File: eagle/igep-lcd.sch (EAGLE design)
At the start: 36 parts, among them IC1 LM1117IMPX-3.3, U1 SN74LVC8T245PW, U2 SN74LVC8T245PW, U3 SN74LVC8T245PW, U4 SN74LVC8T245PW

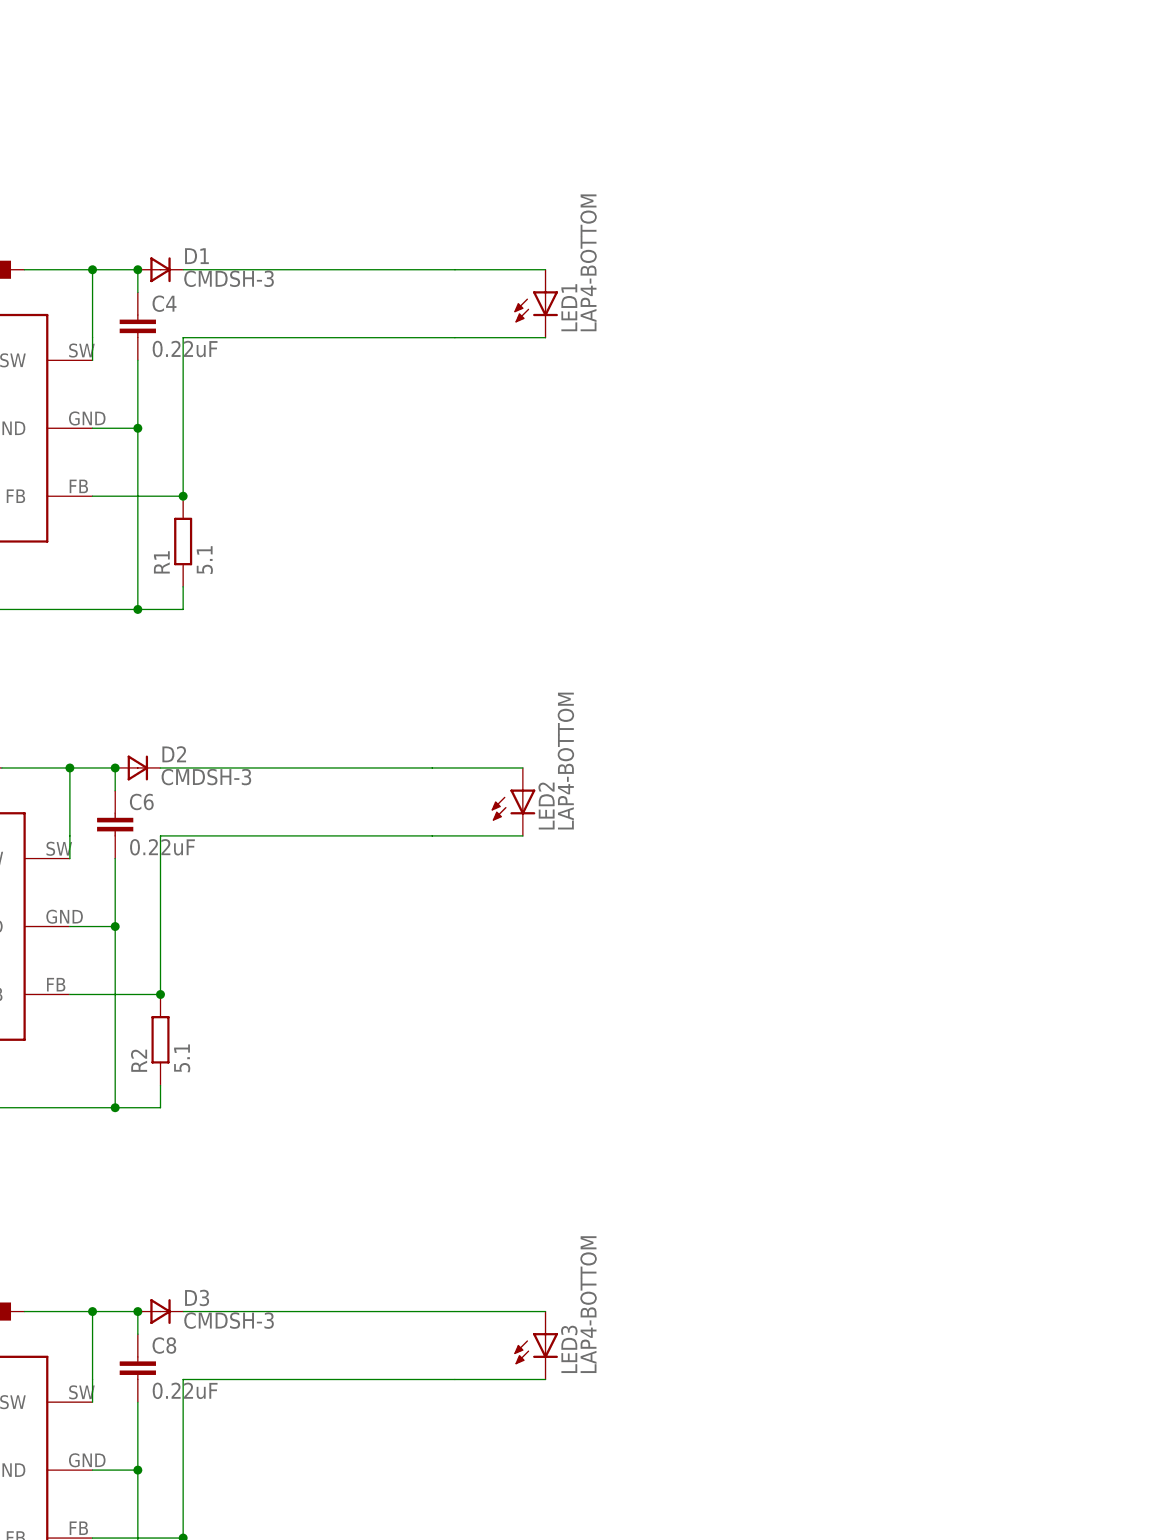
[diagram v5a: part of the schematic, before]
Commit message: Added backlight connectors
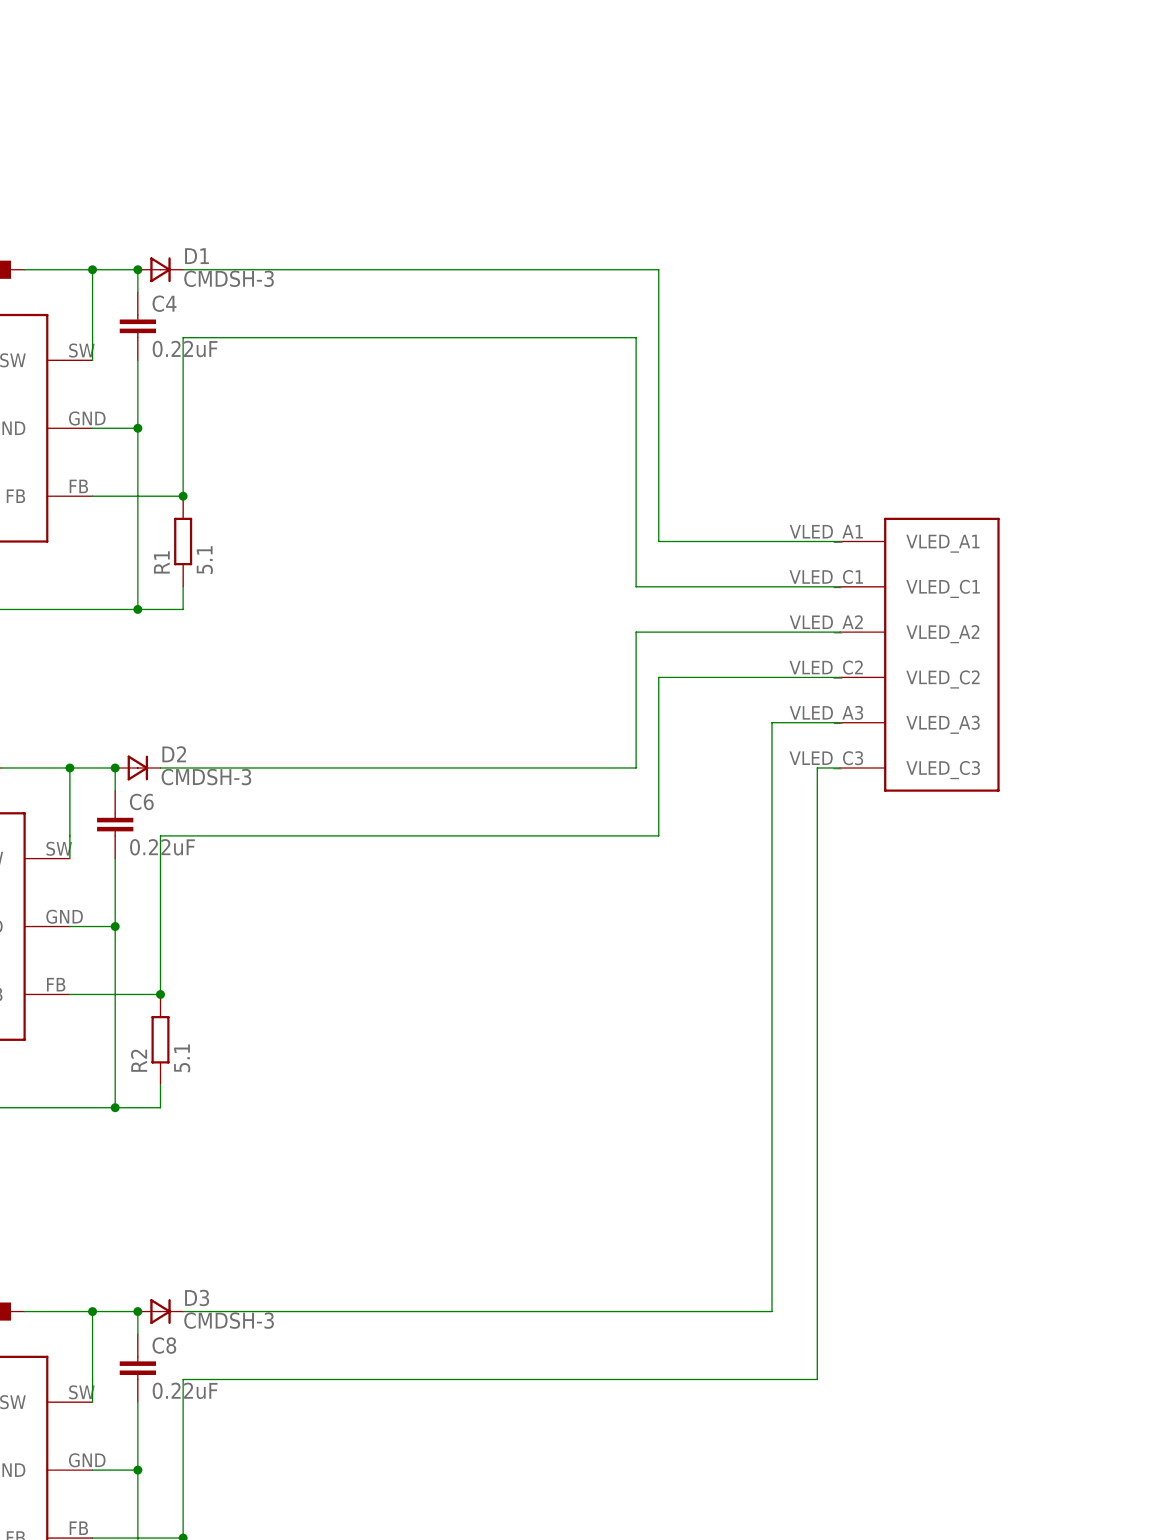
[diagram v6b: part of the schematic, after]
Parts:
- removed LED1, LED2, LED3: LAP4-BOTTOM, led:LAP4-BOTTOM
- added U$5: LCD_BL, lcd-bl:LCD_BL
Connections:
- net N$13: now also U$5.VLED_A1; no longer LED1.A
- net N$14: now also U$5.VLED_C1; no longer LED1.C
- net N$16: now also U$5.VLED_A2; no longer LED2.A
- net N$17: now also U$5.VLED_C2; no longer LED2.C
- net N$22: now also U$5.VLED_A3; no longer LED3.A
- net N$23: now also U$5.VLED_C3; no longer LED3.C
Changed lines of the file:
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@@
 <part name="C4" library="resistor" deviceset="C-EU" device="025-024X044" value="0.22uF"/>
 <part name="R1" library="resistor" deviceset="R-EU_" device="0204/2V" value="5.1"/>
-<part name="LED1" library="led" deviceset="*P4" device="-BOTTOM" technology="LA"/>
 <part name="BL_5VOLT_1" library="testpad" deviceset="TP" device="B1,27"/>
 <part name="BL_PWM_1" library="testpad" deviceset="TP" device="B1,27"/>
@@
 <part name="C6" library="resistor" deviceset="C-EU" device="025-024X044" value="0.22uF"/>
 <part name="R2" library="resistor" deviceset="R-EU_" device="0204/2V" value="5.1"/>
-<part name="LED2" library="led" deviceset="*P4" device="-BOTTOM" technology="LA"/>
 <part name="BL_5VOLT_2" library="testpad" deviceset="TP" device="B1,27"/>
 <part name="BL_PWM_2" library="testpad" deviceset="TP" device="B1,27"/>
@@
 <part name="C8" library="resistor" deviceset="C-EU" device="025-024X044" value="0.22uF"/>
 <part name="R3" library="resistor" deviceset="R-EU_" device="0204/2V" value="5.1"/>
-<part name="LED3" library="led" deviceset="*P4" device="-BOTTOM" technology="LA"/>
 <part name="BL_5VOLT_3" library="testpad" deviceset="TP" device="B1,27"/>
 <part name="BL_PWM_3" library="testpad" deviceset="TP" device="B1,27"/>
+<part name="U$5" library="lcd-bl" deviceset="LCD_BL" device=""/>
 </parts>
 <sheets>
 <sheet>
+<description>IGEPv2 LCD exp board</description>
 <plain>
 <text x="335.28" y="12.7" size="1.778" layer="91">TODO: Check what's PCI?</text>
@@
 <instance part="C4" gate="G$1" x="124.46" y="-167.64"/>
 <instance part="R1" gate="G$1" x="129.54" y="-193.04" rot="R90"/>
-<instance part="LED1" gate="G$1" x="170.18" y="-165.1"/>
 <instance part="BL_5VOLT_1" gate="G$1" x="81.28" y="-167.64" rot="R180"/>
 <instance part="BL_PWM_1" gate="G$1" x="81.28" y="-172.72"/>
@@
 <instance part="C6" gate="G$1" x="121.92" y="-223.52"/>
 <instance part="R2" gate="G$1" x="127" y="-248.92" rot="R90"/>
-<instance part="LED2" gate="G$1" x="167.64" y="-220.98"/>
 <instance part="BL_5VOLT_2" gate="G$1" x="78.74" y="-223.52" rot="R180"/>
 <instance part="BL_PWM_2" gate="G$1" x="78.74" y="-228.6"/>
@@
 <instance part="C8" gate="G$1" x="124.46" y="-284.48"/>
 <instance part="R3" gate="G$1" x="129.54" y="-309.88" rot="R90"/>
-<instance part="LED3" gate="G$1" x="170.18" y="-281.94"/>
 <instance part="BL_5VOLT_3" gate="G$1" x="81.28" y="-284.48" rot="R180"/>
 <instance part="BL_PWM_3" gate="G$1" x="81.28" y="-289.56"/>
+<instance part="U$5" gate="G$1" x="208.28" y="-231.14" rot="MR270"/>
 </instances>
 <busses>
@@
 <segment>
 <pinref part="D1" gate="G$1" pin="C"/>
-<wire x1="129.54" y1="-162.56" x2="160.02" y2="-162.56" width="0.1524" layer="91"/>
-<pinref part="LED1" gate="G$1" pin="A"/>
-<wire x1="160.02" y1="-162.56" x2="170.18" y2="-162.56" width="0.1524" layer="91"/>
+<wire x1="129.54" y1="-162.56" x2="182.88" y2="-162.56" width="0.1524" layer="91"/>
+<wire x1="203.2" y1="-193.04" x2="182.88" y2="-193.04" width="0.1524" layer="91"/>
+<wire x1="182.88" y1="-193.04" x2="182.88" y2="-162.56" width="0.1524" layer="91"/>
+<pinref part="U$5" gate="G$1" pin="VLED_A1"/>
 </segment>
 </net>
 <net name="N$14" class="0">
 <segment>
-<wire x1="160.02" y1="-170.18" x2="129.54" y2="-170.18" width="0.1524" layer="91"/>
+<wire x1="180.34" y1="-170.18" x2="129.54" y2="-170.18" width="0.1524" layer="91"/>
 <wire x1="129.54" y1="-170.18" x2="129.54" y2="-187.96" width="0.1524" layer="91"/>
 <pinref part="U$2" gate="G$1" pin="FB"/>
@@
 <pinref part="R1" gate="G$1" pin="2"/>
 <junction x="129.54" y="-187.96"/>
-<pinref part="LED1" gate="G$1" pin="C"/>
-<wire x1="170.18" y1="-170.18" x2="160.02" y2="-170.18" width="0.1524" layer="91"/>
+<wire x1="180.34" y1="-170.18" x2="180.34" y2="-198.12" width="0.1524" layer="91"/>
+<pinref part="U$5" gate="G$1" pin="VLED_C1"/>
+<wire x1="180.34" y1="-198.12" x2="203.2" y2="-198.12" width="0.1524" layer="91"/>
 </segment>
 </net>
@@
 <segment>
 <pinref part="D2" gate="G$1" pin="C"/>
-<wire x1="127" y1="-218.44" x2="157.48" y2="-218.44" width="0.1524" layer="91"/>
-<pinref part="LED2" gate="G$1" pin="A"/>
-<wire x1="157.48" y1="-218.44" x2="167.64" y2="-218.44" width="0.1524" layer="91"/>
+<wire x1="127" y1="-218.44" x2="180.34" y2="-218.44" width="0.1524" layer="91"/>
+<pinref part="U$5" gate="G$1" pin="VLED_A2"/>
+<wire x1="203.2" y1="-203.2" x2="180.34" y2="-203.2" width="0.1524" layer="91"/>
+<wire x1="180.34" y1="-203.2" x2="180.34" y2="-218.44" width="0.1524" layer="91"/>
 </segment>
 </net>
 <net name="N$17" class="0">
 <segment>
-<wire x1="157.48" y1="-226.06" x2="127" y2="-226.06" width="0.1524" layer="91"/>
+<wire x1="182.88" y1="-226.06" x2="127" y2="-226.06" width="0.1524" layer="91"/>
 <wire x1="127" y1="-226.06" x2="127" y2="-243.84" width="0.1524" layer="91"/>
 <pinref part="U$3" gate="G$1" pin="FB"/>
@@
 <pinref part="R2" gate="G$1" pin="2"/>
 <junction x="127" y="-243.84"/>
-<pinref part="LED2" gate="G$1" pin="C"/>
-<wire x1="167.64" y1="-226.06" x2="157.48" y2="-226.06" width="0.1524" layer="91"/>
+<wire x1="182.88" y1="-226.06" x2="182.88" y2="-208.28" width="0.1524" layer="91"/>
+<pinref part="U$5" gate="G$1" pin="VLED_C2"/>
+<wire x1="182.88" y1="-208.28" x2="203.2" y2="-208.28" width="0.1524" layer="91"/>
 </segment>
 </net>
@@
 <segment>
 <pinref part="D3" gate="G$1" pin="C"/>
-<wire x1="129.54" y1="-279.4" x2="160.02" y2="-279.4" width="0.1524" layer="91"/>
-<pinref part="LED3" gate="G$1" pin="A"/>
-<wire x1="160.02" y1="-279.4" x2="170.18" y2="-279.4" width="0.1524" layer="91"/>
+<wire x1="129.54" y1="-279.4" x2="195.58" y2="-279.4" width="0.1524" layer="91"/>
+<wire x1="195.58" y1="-279.4" x2="195.58" y2="-213.36" width="0.1524" layer="91"/>
+<pinref part="U$5" gate="G$1" pin="VLED_A3"/>
+<wire x1="195.58" y1="-213.36" x2="203.2" y2="-213.36" width="0.1524" layer="91"/>
 </segment>
 </net>
 <net name="N$23" class="0">
 <segment>
-<wire x1="160.02" y1="-287.02" x2="129.54" y2="-287.02" width="0.1524" layer="91"/>
+<wire x1="200.66" y1="-287.02" x2="129.54" y2="-287.02" width="0.1524" layer="91"/>
 <wire x1="129.54" y1="-287.02" x2="129.54" y2="-304.8" width="0.1524" layer="91"/>
 <pinref part="U$4" gate="G$1" pin="FB"/>
@@
 <pinref part="R3" gate="G$1" pin="2"/>
 <junction x="129.54" y="-304.8"/>
-<pinref part="LED3" gate="G$1" pin="C"/>
-<wire x1="170.18" y1="-287.02" x2="160.02" y2="-287.02" width="0.1524" layer="91"/>
-</segment>
-</net>
+<pinref part="U$5" gate="G$1" pin="VLED_C3"/>
+<wire x1="203.2" y1="-218.44" x2="200.66" y2="-218.44" width="0.1524" layer="91"/>
+<wire x1="200.66" y1="-218.44" x2="200.66" y2="-287.02" width="0.1524" layer="91"/>
+</segment>
+</net>

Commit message: Added touchscreen digitizer. TODO: touchscreen connector missing.
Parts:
- added C10: 10uF, rcl:C-EU050-025X075
- added C11, C12, C13, C14, C15, C9: 0.1uF, rcl:C-EU050-025X075
- added C16, C17, C18, C19, C20, C21, C22, C23, C24, C25, C26, C27, C28, C29, C30, C31, C32, C33, C34, C35, C36, C37, C38, C39: 0.1uF, rcl:C-EU050-024X044
- added U$6: ADS7843, ads7843:ADS7843
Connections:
- new net N$1: U$6.DCLK
- new net N$2: C1.2, C10.2, C11.2, C12.2, C13.2, C14.2, C15.2, C2.2, C3.2, C4.2, C5.2, C6.2, C7.2, C8.2, C9.2, IC1.GND, LCD-1.1, LCD-2.1, LCD-29.1, LCD-37.1, LCD-38.1, R1.1, R2.1, R3.1, U$1.GND1, U$1.GND2, U$2.GND, U$3.GND, U$4.GND, U$6.GND, U1.GND, U1.GND_2, U1.GND_3, U1.~OE, U2.GND, U2.GND_2, U2.GND_3, U2.~OE, U3.GND, U3.GND_2, U3.GND_3, U3.~OE, U4.GND, U4.GND_2, U4.GND_3, U4.~OE
- new net N$20: U$1.TS_NPEN_IRQ, U$6.PENIRQ
- new net N$25: U$1.LCD_ENVVDD, U$6.BUSY
- new net N$26: U$1.MCSPI1_SIMO, U$6.DIN
- new net N$27: U$1.MCSPI1_SOMI, U$6.DOUT
- new net N$7: U$6.CS
- net HSYNC\: no longer U$1.HSYNC
- net LCD_DATA0: now also C23.1, C23.2
- net LCD_DATA1: now also C22.1, C22.2
- net LCD_DATA10: now also C29.1, C29.2
- net LCD_DATA11: now also C28.1, C28.2
- net LCD_DATA12: now also C27.1, C27.2
- net LCD_DATA13: now also C26.1, C26.2
- net LCD_DATA14: now also C25.1, C25.2
- net LCD_DATA15: now also C24.1, C24.2
- net LCD_DATA16: now also C39.1, C39.2
- net LCD_DATA17: now also C38.1, C38.2
- net LCD_DATA18: now also C37.1, C37.2
- net LCD_DATA19: now also C36.1, C36.2
- net LCD_DATA2: now also C21.1, C21.2
- net LCD_DATA20: now also C35.1, C35.2
- net LCD_DATA21: now also C34.1, C34.2
- net LCD_DATA22: now also C33.1, C33.2
- net LCD_DATA23: now also C32.1, C32.2
- net LCD_DATA3: now also C20.1, C20.2
- net LCD_DATA4: now also C19.1, C19.2
- net LCD_DATA5: now also C18.1, C18.2
- net LCD_DATA6: now also C17.1, C17.2
- net LCD_DATA7: now also C16.1, C16.2
- net LCD_DATA8: now also C31.1, C31.2
- net LCD_DATA9: now also C30.1, C30.2
- net N$12: now also U$1.HSYNC; no longer C1.2, C2.2, C3.2, C4.2, C5.2, C6.2, C7.2, C8.2, IC1.GND, LCD-1.1, LCD-2.1, LCD-29.1, LCD-37.1, LCD-38.1, R1.1, R2.1, R3.1, U$1.GND1, U$1.GND2, U$2.GND, U$3.GND, U$4.GND, U1.GND, U1.GND_2, U1.GND_3, U1.~OE, U2.GND, U2.GND_2, U2.GND_3, U2.~OE, U3.GND, U3.GND_2, U3.GND_3, U3.~OE, U4.GND, U4.GND_2, U4.GND_3, U4.~OE
- net N$19: now also C10.1, C11.1, C9.1, U$6.VCC1, U$6.VCC2, U$6.VREF
- net N$3: now also C12.1, C13.1, C14.1, C15.1

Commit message: Replaced all RLC elements with SMD packages
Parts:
- removed C1: 22uF, capacitor-wima:C2,5-3
- removed R3: 5.1, resistor:R-EU_0204/2V
- added C40: 100nF, rcl:C-EUC1206
- added R4: 5.1, rcl:R-EU_R1206
- C10: value 10uF -> 0.1uF; device rcl:C-EU050-025X075 -> rcl:C-EUC1206
- C11: value 0.1uF -> 10uF; device rcl:C-EU050-025X075 -> rcl:C-EUC1206
- C13, C14: value 0.1uF -> 100nF; device rcl:C-EU050-025X075 -> rcl:C-EUC1206
- C15: value 0.1uF -> 0.22uF; device rcl:C-EU050-025X075 -> rcl:C-EUC1206
- C16, C17, C18, C19, C20, C21, C22, C23, C24, C25, C26, C27, C28, C29, C30, C31, C32, C33, C34, C35, C36, C37, C38, C39: value 0.1uF -> 100nF; device rcl:C-EU050-024X044 -> rcl:C-EUC1206
- C2: value 10uF -> 22uF; device capacitor-wima:C2,5-3 -> rcl:C-EUC1206
- C3, C4, C5, C6: device resistor:C-EU025-024X044 -> rcl:C-EUC1206
- C7: value 1uF -> 10uF; device resistor:C-EU025-024X044 -> rcl:C-EUC1206
- C8: value 0.22uF -> 1uF; device resistor:C-EU025-024X044 -> rcl:C-EUC1206
- C9: device rcl:C-EU050-025X075 -> rcl:C-EUC1206
- L1, L2, L3: device resistor:L-EU0204/5 -> resistor:R-EU_R1210
- R1, R2: device resistor:R-EU_0204/2V -> rcl:R-EU_R1206
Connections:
- removed net N$12: U$1.HSYNC
- new net N$28: C27.1, U2.B4
- net HSYNC\: now also U$1.HSYNC
- net LCD_DATA0: now also C22.1, C22.2; no longer C23.1, C23.2
- net LCD_DATA1: now also C21.1, C21.2; no longer C22.1, C22.2
- net LCD_DATA10: now also C28.1, C28.2; no longer C29.1, C29.2
- net LCD_DATA11: now also C27.2; no longer C28.1, C28.2, U2.B4
- net LCD_DATA12: now also C26.1, C26.2; no longer C27.1, C27.2
- net LCD_DATA13: now also C25.1, C25.2; no longer C26.1, C26.2
- net LCD_DATA14: now also C23.1, C23.2; no longer C25.1, C25.2
- net LCD_DATA16: now also C38.1, C38.2; no longer C39.1, C39.2
- net LCD_DATA17: now also C37.1, C37.2; no longer C38.1, C38.2
- net LCD_DATA18: now also C36.1, C36.2; no longer C37.1, C37.2
- net LCD_DATA19: now also C35.1, C35.2; no longer C36.1, C36.2
- net LCD_DATA2: now also C20.1, C20.2; no longer C21.1, C21.2
- net LCD_DATA20: now also C34.1, C34.2; no longer C35.1, C35.2
- net LCD_DATA21: now also C33.1, C33.2; no longer C34.1, C34.2
- net LCD_DATA22: now also C32.1, C32.2; no longer C33.1, C33.2
- net LCD_DATA23: now also C31.1, C31.2; no longer C32.1, C32.2
- net LCD_DATA3: now also C19.1, C19.2; no longer C20.1, C20.2
- net LCD_DATA4: now also C18.1, C18.2; no longer C19.1, C19.2
- net LCD_DATA5: now also C17.1, C17.2; no longer C18.1, C18.2
- net LCD_DATA6: now also C16.1, C16.2; no longer C17.1, C17.2
- net LCD_DATA7: now also C40.1, C40.2; no longer C16.1, C16.2
- net LCD_DATA8: now also C30.1, C30.2; no longer C31.1, C31.2
- net LCD_DATA9: now also C29.1, C29.2; no longer C30.1, C30.2
- net N$14: now also R4.2; no longer R1.2
- net N$15: now also C4.1, L1.2; no longer C6.1, L2.1
- net N$17: now also R1.2; no longer R2.2
- net N$19: now also C8.1, L1.1, L2.1, L3.1; no longer C2.1, L1.2, L2.2, L3.2
- net N$2: now also C39.2, R4.1; no longer C1.2, R3.1
- net N$21: now also C6.1, L3.2; no longer C8.1, L3.1
- net N$23: now also R2.2; no longer R3.2
- net N$3: now also C2.1, C39.1; no longer C1.1, C15.1
- net N$8: now also C15.1, L2.2; no longer C4.1, L1.1
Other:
- moved on the sheet: C10, C11, C14, C15, C16, C17, C18, C19, C2, C20, C21, C22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
